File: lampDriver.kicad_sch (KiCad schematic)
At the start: 56 parts, among them IC8 FAN3100TSX, Q4 BC807, T4 NMOS_GDS-KS_SMD, U1 OPA2356AIDGKR, U3 LM2902

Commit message: alpha prototype
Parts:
- R51: value 10k 0603 -> 18k 0603
- T4: value NMOS_GDS-KS_SMD -> IMBG120R181M2HXTMA1
- TH1: value NTC xxx -> PTC 680R 80°C
- U1: footprint Package_SO:VSSOP-8_3x3mm_P0.65mm -> Package_SO:VSSOP-8_3.0x3.0mm_P0.65mm
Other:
- note added: "90°C = 2.0 V"
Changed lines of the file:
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@@
 	(generator_version "9.99")
 	(paper "A4")
+	(text "90°C = 2.0 V"
+		(exclude_from_sim no)
+		(at 107.696 67.31 0)
+		(effects
+			(font
+				(size 1.27 1.27)
+			)
+		)
+	)
 	(junction
 		(at 76.2 96.52)
@@
 			)
 		)
-		(property "Footprint" "Package_SO:VSSOP-8_3x3mm_P0.65mm"
+		(property "Footprint" "Package_SO:VSSOP-8_3.0x3.0mm_P0.65mm"
 			(at 250.19 97.79 0)
 			(hide yes)
@@
 			)
 		)
-		(property "Footprint" "Package_SO:VSSOP-8_3x3mm_P0.65mm"
+		(property "Footprint" "Package_SO:VSSOP-8_3.0x3.0mm_P0.65mm"
 			(at 251.46 97.79 0)
 			(hide yes)
@@
 			)
 		)
-		(property "Value" "10k 0603"
+		(property "Value" "18k 0603"
 			(at 121.92 68.5799 0)
 			(effects
@@
 			)
 		)
-		(property "Value" "NMOS_GDS-KS_SMD"
+		(property "Value" "IMBG120R181M2HXTMA1"
 			(at 139.7 87.7569 0)
 			(effects
@@
 			)
 		)
-		(property "Footprint" "Package_SO:VSSOP-8_3x3mm_P0.65mm"
+		(property "Footprint" "Package_SO:VSSOP-8_3.0x3.0mm_P0.65mm"
 			(at 199.39 100.33 0)
 			(hide yes)
@@
 		(on_board yes)
 		(dnp no)
-		(fields_autoplaced yes)
 		(property "Reference" "TH1"
 			(at 121.92 73.9774 0)
@@
 			)
 		)
-		(property "Value" "NTC xxx"
-			(at 121.92 76.5174 0)
+		(property "Value" "PTC 680R 80°C"
+			(at 102.108 74.93 0)
 			(effects
 				(font

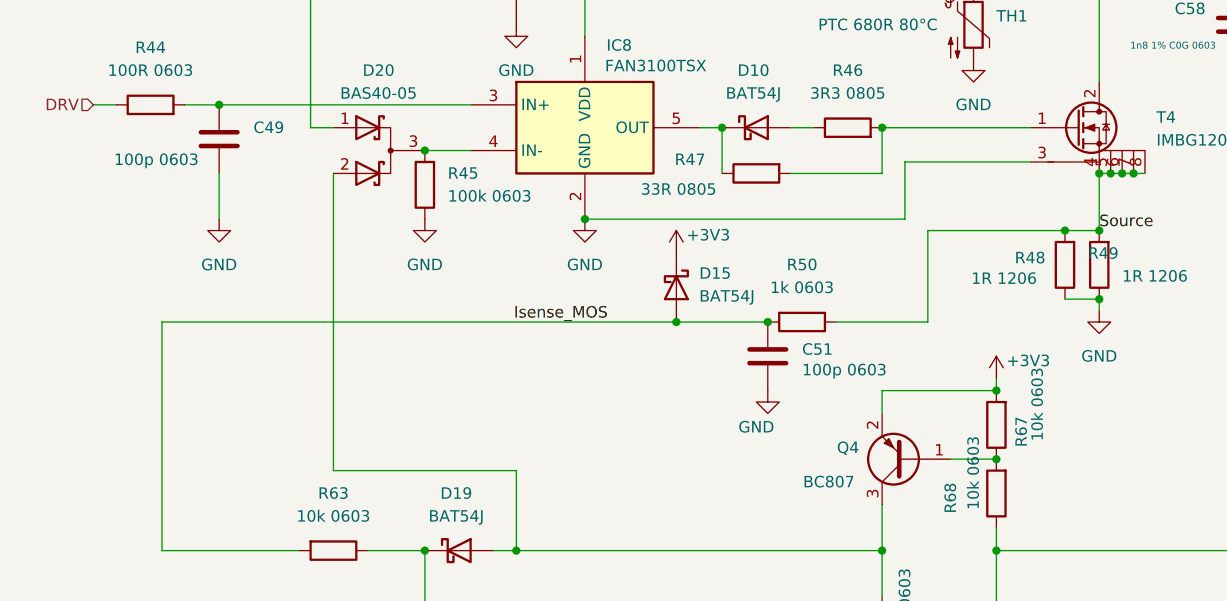
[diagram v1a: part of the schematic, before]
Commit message: error correction first prototype
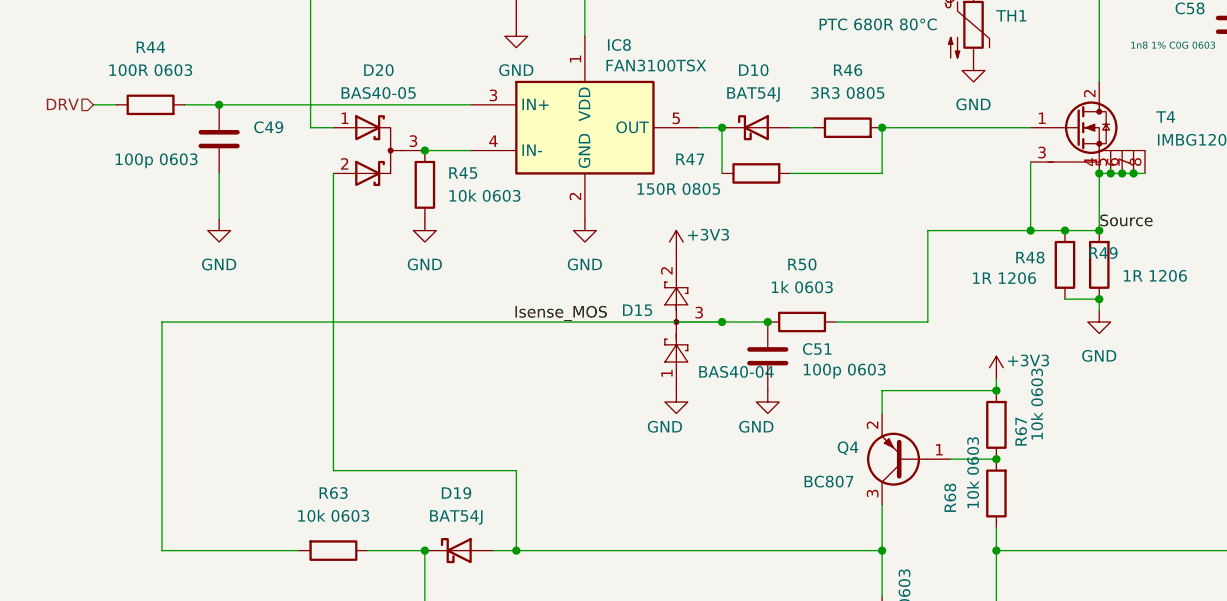
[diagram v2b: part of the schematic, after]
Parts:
- removed D15: BAT54J, Diode_SMD:D_SOD-323F, symbol Diode:BAT54J
- added D15: BAS40-04, Package_TO_SOT_SMD:SOT-23, symbol Diode:BAS40-04
- R45: value 100k 0603 -> 10k 0603
- R47: value 33R 0805 -> 150R 0805
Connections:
- net +3V3: now also D15.2
- net GND: now also D15.1; no longer T4.3 (KS)
- net Isense_MOS: now also D15.3
- net Source: now also T4.3 (KS)
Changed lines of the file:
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@@
 	)
 	(junction
-		(at 76.2 96.52)
-		(diameter 0)
-		(color 0 0 0 0)
-	)
-	(junction
 		(at 67.31 144.78)
 		(diameter 0)
@@
 	)
 	(junction
+		(at 125.73 97.79)
+		(diameter 0)
+		(color 0 0 0 0)
+	)
+	(junction
 		(at 133.35 97.79)
 		(diameter 0)
@@
 	)
 	(junction
-		(at 86.36 107.95)
-		(diameter 0)
-		(color 0 0 0 0)
-	)
-	(junction
 		(at 91.44 86.36)
 		(diameter 0)
@@
 	)
 	(junction
+		(at 91.44 107.95)
+		(diameter 0)
+		(color 0 0 0 0)
+	)
+	(junction
 		(at 58.42 88.9)
 		(diameter 0)
@@
 	(wire
 		(pts
-			(xy 215.9 100.33) (xy 219.71 100.33)
+			(xy 91.44 107.95) (xy 96.52 107.95)
 		)
 		(stroke
@@
 	(wire
 		(pts
-			(xy 137.16 91.44) (xy 138.43 91.44)
+			(xy 215.9 100.33) (xy 219.71 100.33)
 		)
 		(stroke
@@
 	(wire
 		(pts
-			(xy 148.59 48.26) (xy 153.67 48.26)
+			(xy 137.16 91.44) (xy 138.43 91.44)
 		)
 		(stroke
-			(width 0.254)
+			(width 0)
 			(type default)
 		)
@@
 	(wire
 		(pts
-			(xy 212.09 46.99) (xy 218.44 46.99)
+			(xy 148.59 48.26) (xy 153.67 48.26)
 		)
 		(stroke
-			(width 0)
+			(width 0.254)
 			(type default)
 		)
@@
 	(wire
 		(pts
-			(xy 125.73 90.17) (xy 111.76 90.17)
+			(xy 212.09 46.99) (xy 218.44 46.99)
 		)
 		(stroke
@@
 	(wire
 		(pts
-			(xy 29.21 107.95) (xy 86.36 107.95)
-		)
-		(stroke
-			(width 0)
-			(type default)
-		)
-	)
-	(wire
-		(pts
 			(xy 176.53 48.26) (xy 163.83 48.26)
 		)
@@
 	(wire
 		(pts
+			(xy 125.73 90.17) (xy 125.73 97.79)
+		)
+		(stroke
+			(width 0)
+			(type default)
+		)
+	)
+	(wire
+		(pts
 			(xy 190.5 30.48) (xy 271.78 30.48)
 		)
@@
 	(wire
 		(pts
-			(xy 114.3 97.79) (xy 129.54 97.79)
+			(xy 114.3 97.79) (xy 125.73 97.79)
 		)
 		(stroke
@@
 	(wire
 		(pts
-			(xy 76.2 96.52) (xy 111.76 96.52)
-		)
-		(stroke
-			(width 0)
-			(type default)
-		)
-	)
-	(wire
-		(pts
 			(xy 245.11 77.47) (xy 265.43 77.47)
 		)
@@
 	(wire
 		(pts
-			(xy 86.36 107.95) (xy 96.52 107.95)
+			(xy 29.21 107.95) (xy 91.44 107.95)
 		)
 		(stroke
@@
 	(wire
 		(pts
+			(xy 125.73 97.79) (xy 129.54 97.79)
+		)
+		(stroke
+			(width 0)
+			(type default)
+		)
+	)
+	(wire
+		(pts
 			(xy 67.31 38.1) (xy 71.12 38.1)
 		)
@@
 		)
 	)
-	(wire
-		(pts
-			(xy 111.76 90.17) (xy 111.76 96.52)
-		)
-		(stroke
-			(width 0)
-			(type default)
-		)
-	)
 	(label "HV_Drain_div3"
 		(at 148.59 71.12 180)
@@
 	(symbol
 		(lib_id "power:GND")
+		(at 86.36 115.57 0)
+		(unit 1)
+		(exclude_from_sim no)
+		(in_bom yes)
+		(on_board yes)
+		(dnp no)
+		(property "Reference" "#PWR089"
+			(at 86.36 121.92 0)
+			(hide yes)
+			(effects
+				(font
+					(size 1.27 1.27)
+				)
+			)
+		)
+		(property "Value" "GND"
+			(at 85.09 119.634 0)
+			(effects
+				(font
+					(size 1.27 1.27)
+				)
+			)
+		)
+		(property "Footprint" ""
+			(at 86.36 115.57 0)
+			(hide yes)
+			(effects
+				(font
+					(size 1.27 1.27)
+				)
+			)
+		)
+		(property "Datasheet" ""
+			(at 86.36 115.57 0)
+			(hide yes)
+			(effects
+				(font
+					(size 1.27 1.27)
+				)
+			)
+		)
+		(property "Description" "Power symbol creates a global label with name \"GND\" , ground"
+			(at 86.36 115.57 0)
+			(hide yes)
+			(effects
+				(font
+					(size 1.27 1.27)
+				)
+			)
+		)
+		(pin "1"
+		)
+		(instances
+			(project "OSLUV"
+				(path "/c6e900e0-9399-44f0-8089-9dd7b8ffe54c/9b3070c3-43e0-4d43-9da1-9bc1bd2d6fb9/8926c1e3-dcc6-4ec7-96ae-5bdb4f87d364"
+					(reference "#PWR089")
+					(unit 1)
+				)
+			)
+		)
+	)
+	(symbol
+		(lib_id "power:GND")
 		(at 241.3 73.66 0)
 		(unit 1)
@@
 			)
 		)
-		(property "Value" "100k 0603"
+		(property "Value" "10k 0603"
 			(at 60.96 93.9799 0)
 			(effects
@@
 	)
 	(symbol
-		(lib_id "Diode:BAT54J")
-		(at 86.36 104.14 270)
-		(unit 1)
-		(exclude_from_sim no)
-		(in_bom yes)
-		(on_board yes)
-		(dnp no)
-		(fields_autoplaced yes)
-		(property "Reference" "D15"
-			(at 88.9 102.5524 90)
-			(effects
-				(font
-					(size 1.27 1.27)
-				)
-				(justify left)
-			)
-		)
-		(property "Value" "BAT54J"
-			(at 88.9 105.0924 90)
-			(effects
-				(font
-					(size 1.27 1.27)
-				)
-				(justify left)
-			)
-		)
-		(property "Footprint" "Diode_SMD:D_SOD-323F"
-			(at 81.915 104.14 0)
-			(hide yes)
-			(effects
-				(font
-					(size 1.27 1.27)
-				)
-			)
-		)
-		(property "Datasheet" "https://assets.nexperia.com/documents/data-sheet/BAT54J.pdf"
-			(at 86.36 104.14 0)
-			(hide yes)
-			(effects
-				(font
-					(size 1.27 1.27)
-				)
-			)
-		)
-		(property "Description" "30V 200mA Schottky diode, SOD-323F"
-			(at 86.36 104.14 0)
-			(hide yes)
-			(effects
-				(font
-					(size 1.27 1.27)
-				)
-			)
-		)
-		(pin "2"
-		)
-		(pin "1"
-		)
-		(instances
-			(project "OSLUV"
-				(path "/c6e900e0-9399-44f0-8089-9dd7b8ffe54c/9b3070c3-43e0-4d43-9da1-9bc1bd2d6fb9/8926c1e3-dcc6-4ec7-96ae-5bdb4f87d364"
-					(reference "D15")
-					(unit 1)
-				)
-			)
-		)
-	)
-	(symbol
 		(lib_id "Device:R")
 		(at 100.33 107.95 270)
@@
 	)
 	(symbol
+		(lib_id "Diode:BAS40-04")
+		(at 88.9 107.95 90)
+		(unit 1)
+		(exclude_from_sim no)
+		(in_bom yes)
+		(on_board yes)
+		(dnp no)
+		(property "Reference" "D15"
+			(at 83.82 106.6799 90)
+			(effects
+				(font
+					(size 1.27 1.27)
+				)
+				(justify left)
+			)
+		)
+		(property "Value" "BAS40-04"
+			(at 97.282 113.538 90)
+			(effects
+				(font
+					(size 1.27 1.27)
+				)
+				(justify left)
+			)
+		)
+		(property "Footprint" "Package_TO_SOT_SMD:SOT-23"
+			(at 81.28 114.3 0)
+			(hide yes)
+			(effects
+				(font
+					(size 1.27 1.27)
+				)
+				(justify left)
+			)
+		)
+		(property "Datasheet" "http://www.vishay.com/docs/85701/bas40v.pdf"
+			(at 86.36 110.998 0)
+			(hide yes)
+			(effects
+				(font
+					(size 1.27 1.27)
+				)
+			)
+		)
+		(property "Description" "40V 0.2A Dual Small Signal Schottky Diodes"
+			(at 88.9 107.95 0)
+			(hide yes)
+			(effects
+				(font
+					(size 1.27 1.27)
+				)
+			)
+		)
+		(pin "3"
+		)
+		(pin "1"
+		)
+		(pin "2"
+		)
+		(instances
+			(project "OSLUV"
+				(path "/c6e900e0-9399-44f0-8089-9dd7b8ffe54c/9b3070c3-43e0-4d43-9da1-9bc1bd2d6fb9/8926c1e3-dcc6-4ec7-96ae-5bdb4f87d364"
+					(reference "D15")
+					(unit 1)
+				)
+			)
+		)
+	)
+	(symbol
 		(lib_id "Device:R")
 		(at 105.41 86.36 90)
@@
 			)
 		)
-		(property "Value" "33R 0805"
+		(property "Value" "150R 0805"
 			(at 86.614 93.218 90)
 			(effects

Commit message: etd29 transformer single layer
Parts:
- removed D20: BAS40-05, Package_TO_SOT_SMD:SOT-23, symbol Device:D_Schottky_Dual_CommonCathode_AAK_Parallel
- removed L103: EF25, OSLUV:EF25_outerPinsOnly, symbol OSLUV:EF25_outerPinsOnly
- added C3: 100p 0603, Capacitor_SMD:C_0603_1608Metric, symbol Device:C
- added C4: 100n 0603, Capacitor_SMD:C_0603_1608Metric, symbol Device:C
- added L103: ETD29, OSLUV:ETD29_OSLUV, symbol OSLUV:ETD29
- added R73: 100k 0603, Resistor_SMD:R_0603_1608Metric, symbol Device:R
- added R74: 1k 0603, Resistor_SMD:R_0603_1608Metric, symbol Device:R
- added R75: 10k 0603, Resistor_SMD:R_0603_1608Metric, symbol Device:R
- added R76: 2k2 0603, Resistor_SMD:R_0603_1608Metric, symbol Device:R
- added unit 2 of U3
- R48, R49: value 1R 1206 -> 0R47 1206
- R51: value 18k 0603 -> 1k8 0603
- R52: value 82R 1206/MMA -> 22R 1206/MMA
- R53: value 51R 0603 -> 56R 0603
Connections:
- net +3V3: now also R75.1
- net GND: now also C3.2, C4.2, L103.10, R73.2, R76.1
- net HV_Drain: now also L103.8
- net Isense_Lamp: now also R73.1
- net Lamp_HV: now also L103.2
- net OCP: now also U3.7
- net Usense_Lamp: now also C4.1, R74.1; no longer U1.1, U1.2 (-)
- net VDC_Trafo: now also L103.5
- net temp_MOSFET: now also C3.1, U3.6 (-)
- net at IC8.4 (IN-), R45.2: now also D19.2 (A), Q4.3 (C), R69.2
- new net: R74.2, U1.1, U1.2 (-)
- new net: R75.2, R76.2, U3.5 (+)
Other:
- note added: "90°C = 3.1 V"
- note removed: "90°C = 2.0 V"
- moved on the sheet: C54, C55, C56, C57, C58, C59, R48, R49, R51, R54, R55, R56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
